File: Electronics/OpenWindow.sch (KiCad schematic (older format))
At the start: 28 parts

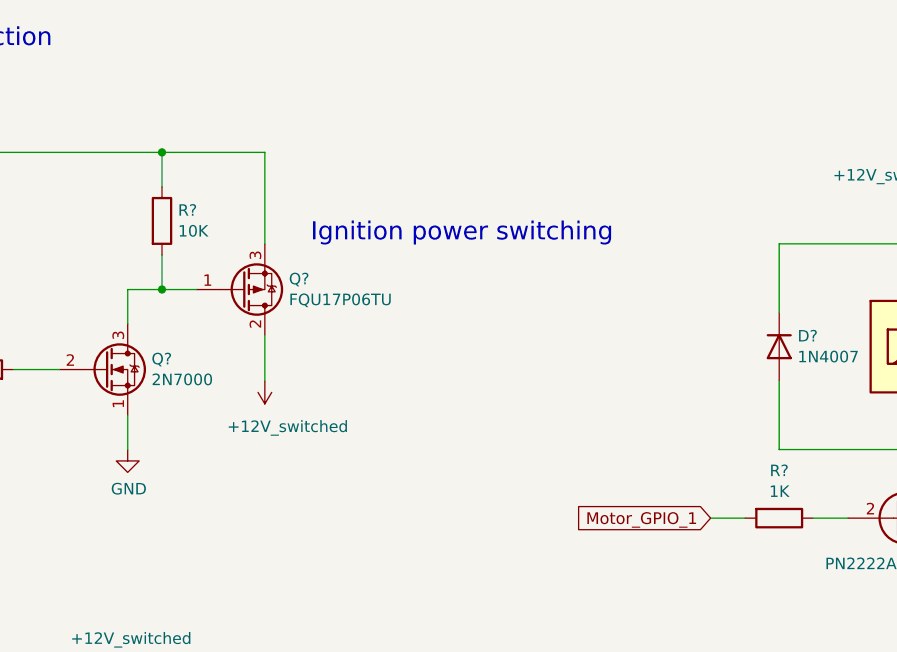
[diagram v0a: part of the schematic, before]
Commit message: Minor schematic changes
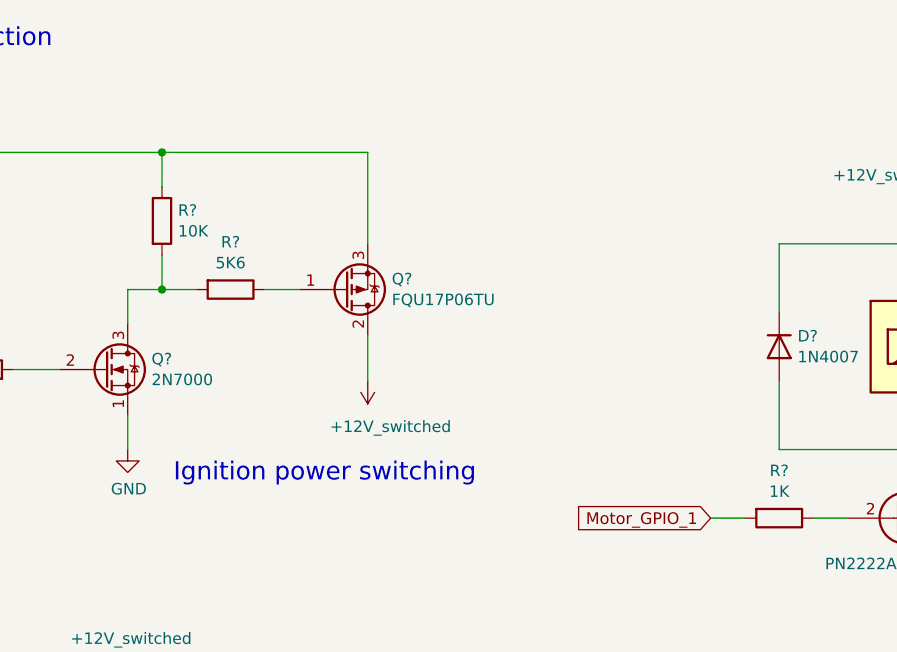
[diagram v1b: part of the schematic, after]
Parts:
- added R?: 5K6, symbol Device:R
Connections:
- net at Q?.3 (D), R?.2: now also R?.2; no longer Q?.1 (G)
- new net: Q?.1 (G), R?.1
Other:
- moved on the sheet: Q?
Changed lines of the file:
@@
 encoding utf-8
 Sheet 1 1
-Title "OpenWindow schematic"
+Title "OpenWindow dev board schematic"
 Date ""
 Rev "1"
@@
 L OpenWindow:FQU17P06TU Q?
 U 1 1 5F8CC278
-P 4350 1850
-F 0 "Q?" H 4555 1804 50  0000 L CNN
-F 1 "FQU17P06TU" H 4555 1895 50  0000 L CNN
-F 2 "Package_TO_SOT_THT:TO-251-3_Vertical" H 4550 1950 50  0001 C CNN
-F 3 "http://www.farnell.com/datasheets/2304440.pdf" H 4350 1850 50  0001 C CNN
-	1    4350 1850
+P 4800 1850
+F 0 "Q?" H 5005 1804 50  0000 L CNN
+F 1 "FQU17P06TU" H 5005 1895 50  0000 L CNN
+F 2 "Package_TO_SOT_THT:TO-251-3_Vertical" H 5000 1950 50  0001 C CNN
+F 3 "http://www.farnell.com/datasheets/2304440.pdf" H 4800 1850 50  0001 C CNN
+	1    4800 1850
 	1    0    0    1
 $EndComp
@@
 L OpenWindow:+12V_switched #PWR?
 U 1 1 5F8DEEA3
-P 4450 2250
-F 0 "#PWR?" H 4450 2100 50  0001 C CNN
-F 1 "+12V_switched" H 4350 2450 50  0000 C CNN
-F 2 "" H 4450 2250 50  0001 C CNN
-F 3 "" H 4450 2250 50  0001 C CNN
-	1    4450 2250
+P 4900 2250
+F 0 "#PWR?" H 4900 2100 50  0001 C CNN
+F 1 "+12V_switched" H 4800 2450 50  0000 C CNN
+F 2 "" H 4900 2250 50  0001 C CNN
+F 3 "" H 4900 2250 50  0001 C CNN
+	1    4900 2250
 	-1   0    0    1
 $EndComp
@@
 	4000 1400 4000 1250
 Wire Wire Line
-	4000 1250 4450 1250
-Wire Wire Line
-	4450 1250 4450 1650
-Wire Wire Line
-	4450 2050 4450 2250
+	4900 1250 4900 1650
+Wire Wire Line
+	4900 2050 4900 2250
 Wire Wire Line
 	3850 2550 3850 2400
@@
 Wire Wire Line
 	2800 2200 3050 2200
-Connection ~ 4000 1250
 Wire Wire Line
 	1350 3200 1500 3200
@@
 Text Notes 2650 800  0    79   ~ 0
 Input protection
-Text Notes 4650 1650 0    79   ~ 0
+Text Notes 4050 2700 0    79   ~ 0
 Ignition power switching
 Text Notes 1600 5700 0    79   ~ 0
@@
 Wire Wire Line
 	4300 5150 4300 5000
+$Comp
+L Device:R R?
+U 1 1 5F855424
+P 4300 1850
+F 0 "R?" V 4093 1850 50  0000 C CNN
+F 1 "5K6" V 4184 1850 50  0000 C CNN
+F 2 "" V 4230 1850 50  0001 C CNN
+F 3 "~" H 4300 1850 50  0001 C CNN
+	1    4300 1850
+	0    1    1    0
+$EndComp
+Wire Wire Line
+	4450 1850 4600 1850
+Wire Wire Line
+	4000 1250 4900 1250
+Connection ~ 4000 1250
 $EndSCHEMATC
